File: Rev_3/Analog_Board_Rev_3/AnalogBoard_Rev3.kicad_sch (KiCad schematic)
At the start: 66 parts, among them J1 Conn_01x06_Male, J2 Conn_01x10_Male, J3 Conn_01x06_Male, J4 Conn_01x08_Male, SW1 SW_DIP_x04, U1 OPA2134, U10 OPA2134, U11 OPA2134, U12 NSL-32, U13 NSL-32, U2 OPA2134, U3 OPA2134, U4 OPA2134, U5 OPA2134, U6 NSL-32, U7 NSL-32, U8 NSL-32, U9 NSL-32

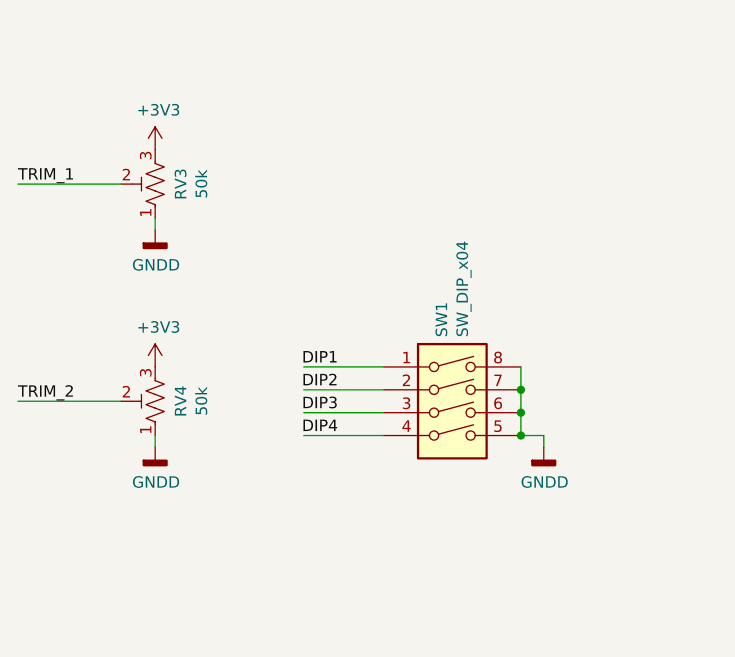
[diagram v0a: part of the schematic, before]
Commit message: Pivoting to Passive Jack Boards
Finalized layout for input/output Jack Boards, which are now completely passive and connected with board-to-board connectors. Schematics are not updated yet, just figuring out placement/dimensions.
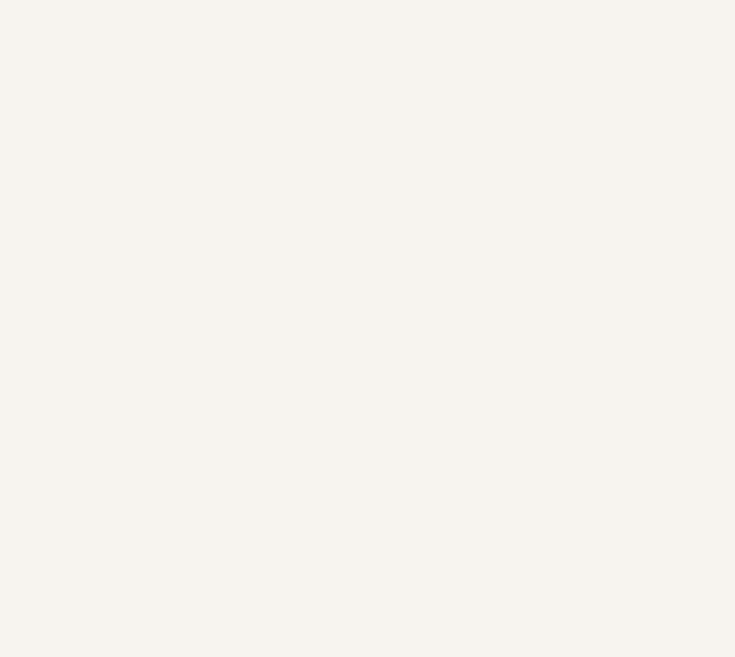
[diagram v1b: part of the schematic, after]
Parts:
- removed RV3, RV4: 50k, Pinebox:Potentiometer_Bourns_3386F_Vertical, symbol AnalogBoard_Rev2-rescue:R_POT_TRIM_US-Device
- removed SW1: SW_DIP_x04, Button_Switch_SMD:SW_DIP_SPSTx04_Slide_6.7x11.72mm_W8.61mm_P2.54mm_LowProfile, symbol Switch:SW_DIP_x04

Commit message: Added analog board back, switched to Jacks on Bottom
Added analog board mezzanine back to fit everything. Finalized decision on jack boards; jacks on bottom, wire to board connectors between jack boards and digital board. Tentative board outlines defined and scoped out component placement.
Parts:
- removed C1, C2: 47n, Capacitor_THT:C_Rect_L7.2mm_W4.5mm_P5.00mm_FKS2_FKP2_MKS2_MKP2, symbol Device:C
- removed C10: 4.7u, Capacitor_THT:CP_Radial_D5.0mm_P2.00mm, symbol Device:C
- removed C11: 47u, Capacitor_THT:CP_Radial_D5.0mm_P2.00mm, symbol Device:C
- removed C12, C13, C14, C15, C16, C17, C18, C23, C24, C3, C6, C9: 100n, Capacitor_SMD:C_0805_2012Metric_Pad1.18x1.45mm_HandSolder, symbol Device:C
- removed C19, C20: 10u, Capacitor_SMD:C_1210_3225Metric_Pad1.33x2.70mm_HandSolder, symbol Device:C
- removed C21, C22: 470n, Capacitor_THT:C_Rect_L7.2mm_W3.5mm_P5.00mm_FKS2_FKP2_MKS2_MKP2, symbol #gplm:cap/CAP-0003-0004
- removed C4, C5, C7, C8: 1n, Capacitor_THT:C_Rect_L7.2mm_W4.5mm_P5.00mm_FKS2_FKP2_MKS2_MKP2, symbol Device:C
- removed D2, D3: 1N914, Diode_THT:D_DO-35_SOD27_P7.62mm_Horizontal, symbol Device:D
- removed D4: D_Zener, Diode_THT:D_DO-34_SOD68_P7.62mm_Horizontal, symbol Device:D_Zener
- removed J1, J3: Conn_01x06_Male, Connector_PinHeader_2.54mm:PinHeader_1x06_P2.54mm_Vertical, symbol Connector:Conn_01x06_Male
- removed J2: Conn_01x10_Male, Connector_PinHeader_2.54mm:PinHeader_1x10_P2.54mm_Vertical, symbol Connector:Conn_01x10_Male
- removed J4: Conn_01x08_Male, Connector_PinHeader_2.54mm:PinHeader_1x08_P2.54mm_Vertical, symbol Connector:Conn_01x08_Male
- removed R1, R2: 1M, Resistor_THT:R_Axial_DIN0207_L6.3mm_D2.5mm_P7.62mm_Horizontal, symbol Device:R
- removed R10: 47k, Resistor_THT:R_Axial_DIN0207_L6.3mm_D2.5mm_P7.62mm_Horizontal, symbol Device:R
- removed R11, R12, R13: 1k, Resistor_THT:R_Axial_DIN0207_L6.3mm_D2.5mm_P7.62mm_Horizontal, symbol Device:R
- removed R14, R16: 560, BB_Resistors:R_Axial_DIN0207_L6.3mm_D2.5mm_P7.5mm_Horizontal, symbol #gplm:res/RES-0001-0034
- removed R15, R17: 33k, BB_Resistors:R_Axial_DIN0207_L6.3mm_D2.5mm_P7.5mm_Horizontal, symbol #gplm:res/RES-0001-0055
- removed R3, R4, R6, R7: 470k, Resistor_THT:R_Axial_DIN0207_L6.3mm_D2.5mm_P7.62mm_Horizontal, symbol Device:R
- removed R5: 3.3k, Resistor_THT:R_Axial_DIN0207_L6.3mm_D2.5mm_P7.62mm_Horizontal, symbol Device:R
- removed R8: 100k, Resistor_THT:R_Axial_DIN0207_L6.3mm_D2.5mm_P7.62mm_Horizontal, symbol Device:R
- removed R9: 10k, Resistor_THT:R_Axial_DIN0207_L6.3mm_D2.5mm_P7.62mm_Horizontal, symbol Device:R
- removed RV1, RV2: 50k, Pinebox:Potentiometer_Bourns_3386F_Vertical, symbol AnalogBoard_Rev2-rescue:R_POT_TRIM_US-Device
- removed U1, U10, U11, U2, U3, U4, U5: OPA2134, Package_DIP:DIP-8_W7.62mm, symbol Amplifier_Operational:OPA2134
- removed U12, U13, U6, U7, U8, U9: NSL-32, Pinebox:Luna_NSL-32_Vertical, symbol Isolator:NSL-32

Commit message: Backing up before windows crash debug
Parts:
- added C21: 100u, Capacitor_SMD:CP_Elec_8x6.2, symbol #gplm:cap/CAP-3005-100U
- added C22, C24: 22n, Capacitor_THT:C_Rect_L7.2mm_W3.0mm_P5.00mm_FKS2_FKP2_MKS2_MKP2, symbol #gplm:cap/CAP-1002-0003
- added C23: 10u, Capacitor_SMD:C_1206_3216Metric, symbol #gplm:cap/CAP-4006-010U
- added C25, C33: 1u, Capacitor_SMD:C_0603_1608Metric, symbol #gplm:cap/CAP-4004-001U
- added C26, C27: 22p, Capacitor_SMD:C_0402_1005Metric, symbol #gplm:cap/CAP-4001-022P
- added C30, C32, C36, C37, C40, C41, C42, C43, C44, C45: 100n, Capacitor_SMD:C_0402_1005Metric, symbol #gplm:cap/RES-4003-100N
- added C31: 10u, Capacitor_SMD:CP_Elec_6.3x5.8, symbol #gplm:cap/CAP-3005-010U
- added C34, C35, C38, C39: 10n, Capacitor_THT:C_Rect_L7.2mm_W3.0mm_P5.00mm_FKS2_FKP2_MKS2_MKP2, symbol #gplm:cap/CAP-1002-0001
- added OP1, OP2, OP3, OP4, OP5, OP6: NSL-32, g-opt:Luna_NSL-32_Vertical, symbol #gplm:opt/OPT-0002-0001
- added R20: 1, Resistor_SMD:R_0603_1608Metric, symbol #gplm:res/RES-2001-001R
- added R21, R22, R23, R24: 1M, Resistor_SMD:R_0603_1608Metric, symbol #gplm:res/RES-2001-001M
- added R25, R26: 100k, Resistor_SMD:R_0603_1608Metric, symbol #gplm:res/RES-2001-100K
- added R27, R28, R29, R30: 39k, Resistor_SMD:R_0603_1608Metric, symbol #gplm:res/RES-2001-039K
- added R31, R32: 100, Resistor_SMD:R_0603_1608Metric, symbol #gplm:res/RES-2001-100R
- added R33, R34: 330, Resistor_SMD:R_0603_1608Metric, symbol #gplm:res/RES-2001-330R
- added RV5, RV6: B1k, g-pot:Potentiometer_Bourns_3214G_Horizontal, symbol #gplm:pot/POT-0008-B102
- added U10, U11, U12, U13, U9: OPA1688IDR, Package_SO:SOIC-8_3.9x4.9mm_P1.27mm, symbol #gplm:ana/ANA-1001-2000
- added U8: TLE2426xD, Package_SO:SOIC-8_3.9x4.9mm_P1.27mm, symbol Reference_Voltage:TLE2426xD
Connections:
- new net: C27.1, R26.2, U9.3 (+)
- new net: OP5.3 (R), R33.1, RV5.1, U13.6 (-)
- new net: OP6.3 (R), R34.1, RV6.1, U13.2 (-)
- new net: C24.2, R24.1, R26.1
- new net: C25.1, U8.8 (NOISE_REDUCTION)
- new net: C26.1, R25.2, U10.3 (+)
- new net: C22.2, R23.1, R25.1
- new net AGND: C21.2, C23.2, C25.2, C30.2, C31.2, C32.2, C33.2, C36.2, C37.2, C40.2, C41.2, C42.2, C43.2, C44.2, C45.2, R21.2, R22.2, U10.4 (V-), U11.4 (V-), U12.4 (V-), U13.4 (V-), U8.2 (COMMON), U9.4 (V-)
- new net BYP_L: C34.1, R27.1, U9.1, U9.2 (-)
- new net BYP_R: C35.1, R28.1, U10.1, U10.2 (-)
- new net DGND: OP1.2 (K), OP2.2 (K), OP3.2 (K), OP4.2 (K), OP5.2 (K), OP6.2 (K)
- new net EFF_L: R33.2, RV5.2, U13.7
- new net EFF_R: R34.2, RV6.2, U13.1
- new net HP_L: C34.2, R30.1, U12.5 (+)
- new net HP_OUT_L: OP2.4 (R), U12.6 (-), U12.7
- new net HP_OUT_R: OP4.4 (R), U11.6 (-), U11.7
- new net HP_R: C35.2, R29.1, U11.5 (+)
- new net IN_L: C24.1, R22.1
- new net IN_R: C22.1, R21.1
- new net LP_L: C39.2, R27.2, U12.3 (+)
- new net LP_OUT_L: OP1.4 (R), U12.1, U12.2 (-)
- new net LP_OUT_R: OP3.4 (R), U11.1, U11.2 (-)
- new net LP_R: C38.2, R28.2, U11.3 (+)
- new net PWM_L_HI: OP2.1 (A)
- new net PWM_L_LO: OP1.1 (A)
- new net PWM_L_VOL: OP5.1 (A)
- new net PWM_R_HI: OP4.1 (A)
- new net PWM_R_LO: OP3.1 (A)
- new net PWM_R_VOL: OP6.1 (A)
- new net SUM_L: OP1.3 (R), OP2.3 (R), R31.1, U9.6 (-)
- new net SUM_OUT_L: OP5.4 (R), R31.2, U9.7
- new net SUM_OUT_R: OP6.4 (R), R32.2, U10.7
- new net SUM_R: OP3.3 (R), OP4.3 (R), R32.1, U10.6 (-)
- new net VCC: C21.1, C23.1, C30.1, C36.1, C40.1, C42.1, C44.1, R20.2, U10.8 (V+), U11.8 (V+), U12.8 (V+), U13.8 (V+), U8.3 (IN), U9.8 (V+)
- new net VIN_PROT: R20.1
- new net VREF: C26.2, C27.2, C31.1, C32.1, C33.1, C37.1, C38.1, C39.1, C41.1, C43.1, C45.1, R23.2, R24.2, R29.2, R30.2, U10.5 (+), U13.3 (+), U13.5 (+), U8.1 (OUT), U9.5 (+)
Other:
- note added: "408 Hz"
- note added: "Coupling caps on Output Board"
- note added: "Gives gain of ~1 at 100% duty"
- note added: "OPA1679?"
- note added: "Trimpot just for testing. Install either pot or R22."
